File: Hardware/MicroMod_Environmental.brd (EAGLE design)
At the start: 65 x 38 mm, 43 parts, among them J1 MICROMOD_STANDARD, U1 SGP40, U2 EEPROM, U3 SHTC3, U4 3.3V, U5 STC31

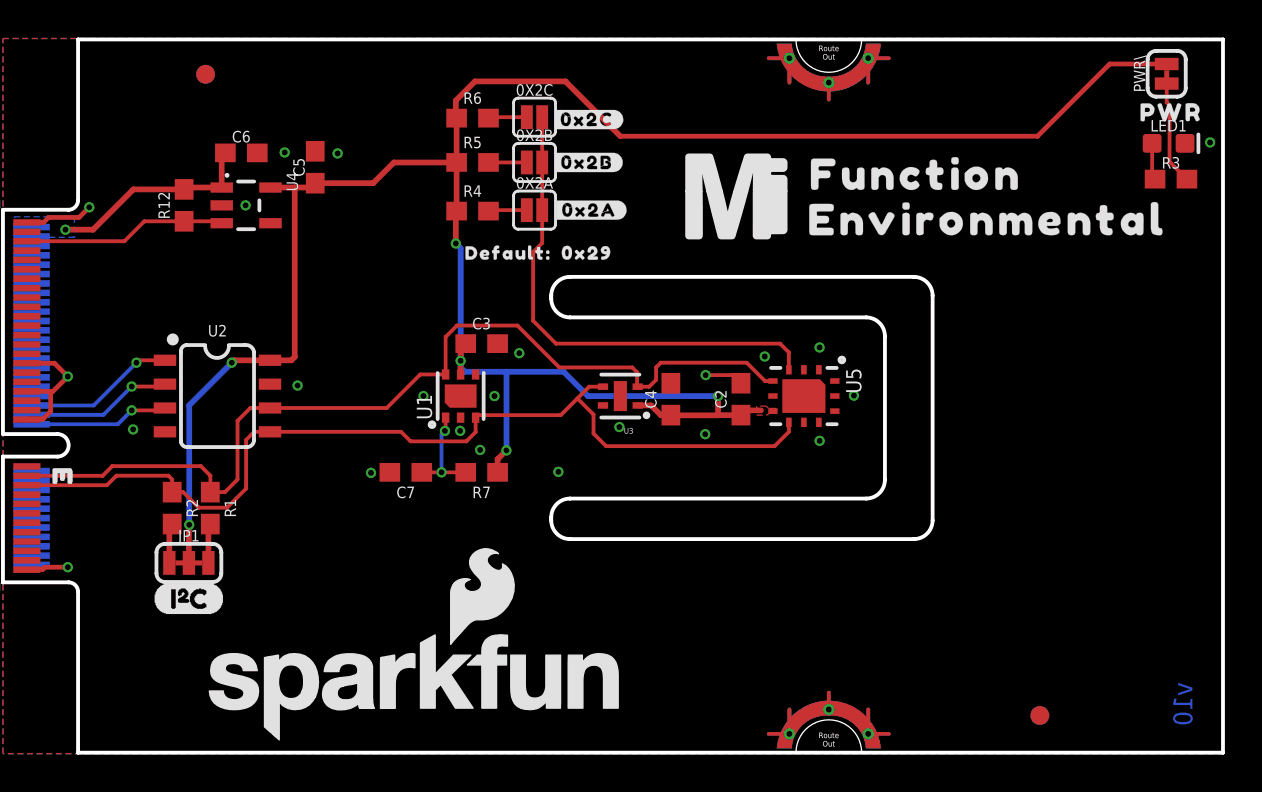
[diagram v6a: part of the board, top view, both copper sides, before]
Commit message: Adds address table in silk, adds a more symmetrical cutout around IC's, labels ICs in silk
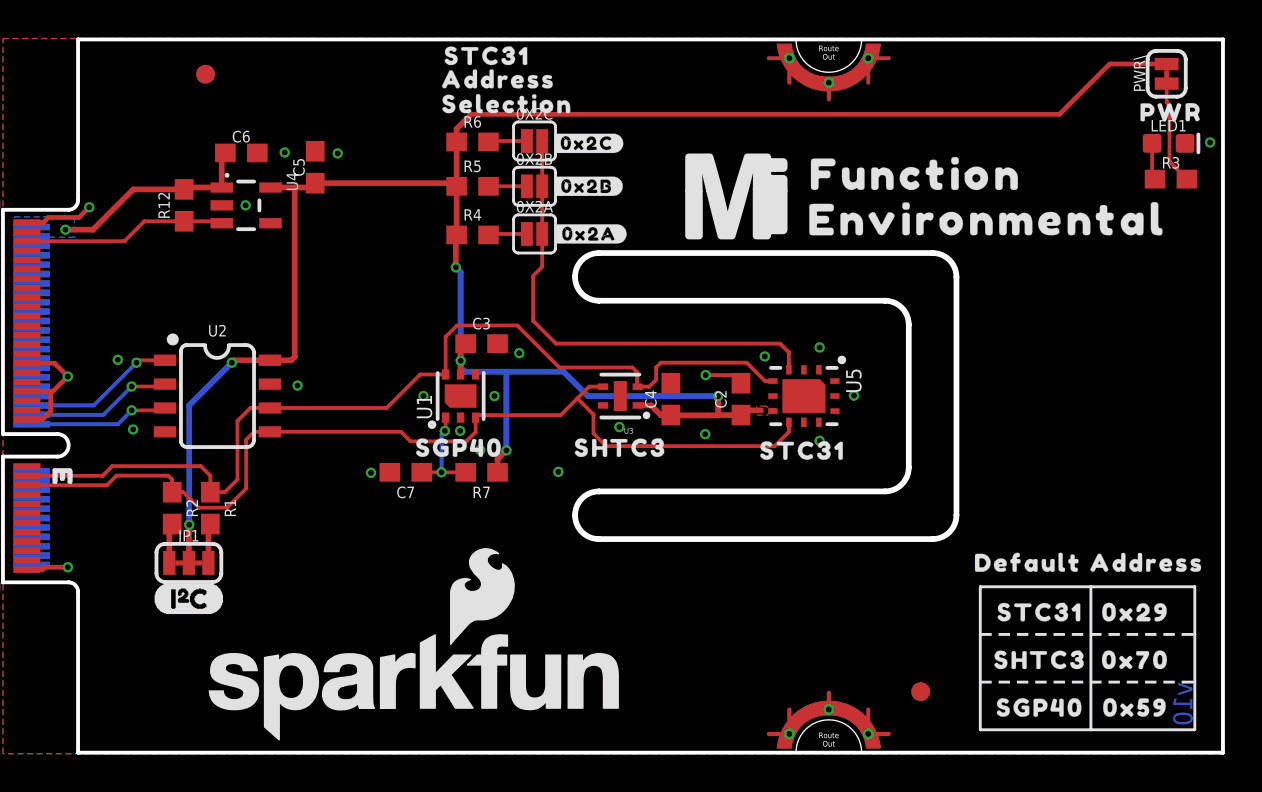
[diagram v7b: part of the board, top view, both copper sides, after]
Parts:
- added LOGO3: SPECIAL_INSTRUCTIONS-ORDERING, SparkFun-Aesthetics:ORDERING_INSTRUCTIONS
- added U$11, U$18: (no value), top:SGP40313503
- added U$12, U$17: (no value), top:SHTC3501
- added U$13, U$16, U$22: (no value), top:STC313502
- added U$14: (no value), top:DEFAULT40313504
- added U$15: (no value), top:ADDRESS40313505
- added U$19: (no value), top:0X5940313520
- added U$20: (no value), top:0X7040313520
- added U$21: (no value), top:SELECTION40313506
- U$10: device top:0X29518 -> top:0X2940313520
- U$9: device top:DEFAULT#518 -> top:ADDRESS40313505
- moved U$10 34.9 mm to (60.4, 7.52)
- moved FRAME1 20.1 mm to (12.7, -17.8)
- moved U$9 9.26 mm to (26.4, 35.9)
- moved FD3 6.48 mm to (48.9, 3.30)
- moved FD4 6.48 mm to (48.9, 3.30)
- moved 0X2A 1.27 mm to (28.3, 27.7)
- moved 0X2B 1.27 mm to (28.3, 30.2)
- moved R4 1.27 mm to (25.0, 27.6)
- moved R5 1.27 mm to (25.0, 30.2)
- moved U$1 1.27 mm to (31.2, 27.7)
- moved U$2 1.27 mm to (31.1, 30.2)
- moved 0X2C 1.27 mm to (28.3, 32.6)
- moved R6 1.27 mm to (25.0, 32.6)
- moved U$3 1.27 mm to (31.1, 32.5)
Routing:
- net 3.3V: track 119.7 -> 115.9 mm
- net ADDR: track 26.3 -> 25.0 mm
- net GND: vias 23 -> 24
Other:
- outline, holes or cut-outs redrawn
- board text added: "0.8mm PCB"
- board text added: "Chamfered Edge"
- board text added: "ENIG Finish"
- board text added: "Elias Santistevan"
